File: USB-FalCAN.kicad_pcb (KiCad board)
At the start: 4 copper layers, 76.5 x 30.9 mm, 58 parts, among them J1 Conn_01x17_Pin, J10 CAN, J2 NC, J3 Conn_01x17_Pin, J4 USB2.0_16P, J5 Boot, J6 NC, J7 DE9_Receptacle, J8 RS-485/422-TX, J9 RS-422-RX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

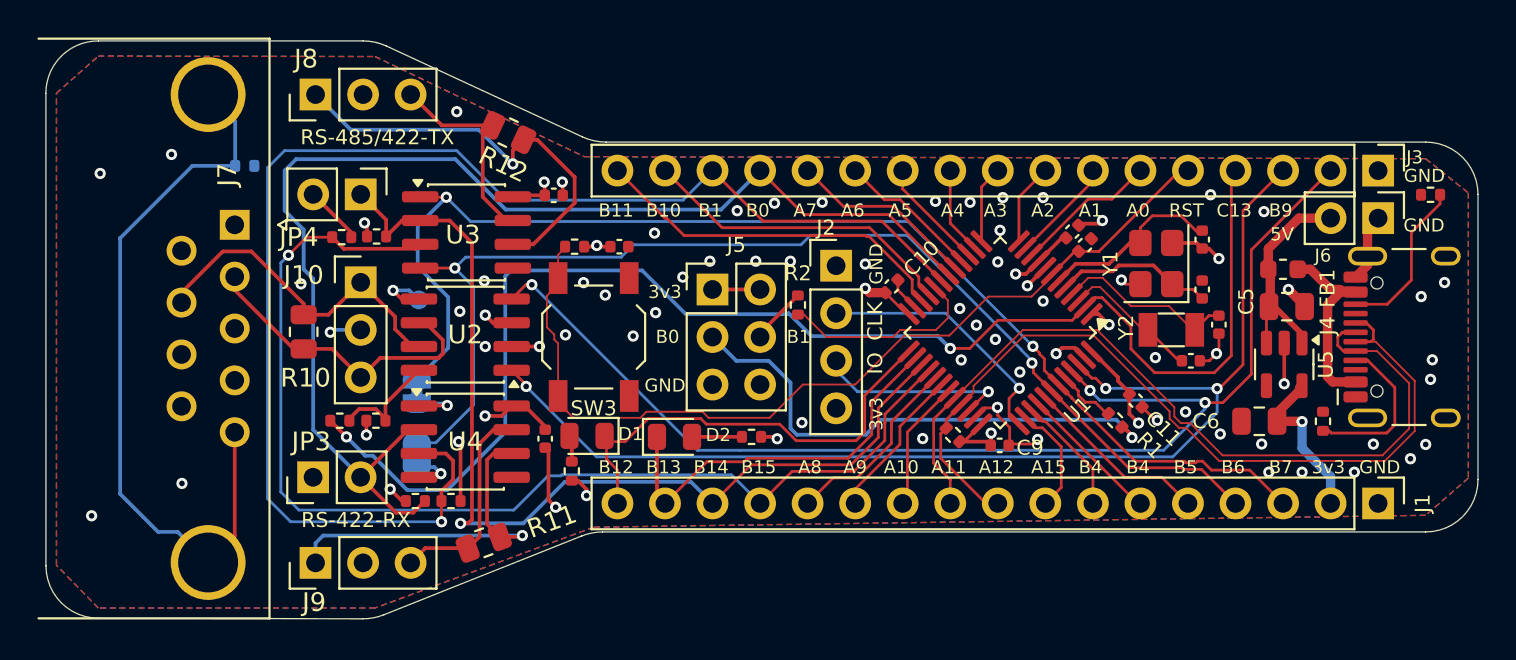
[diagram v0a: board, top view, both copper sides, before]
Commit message: Replace USB-TouCAN files with USB-FalCAN
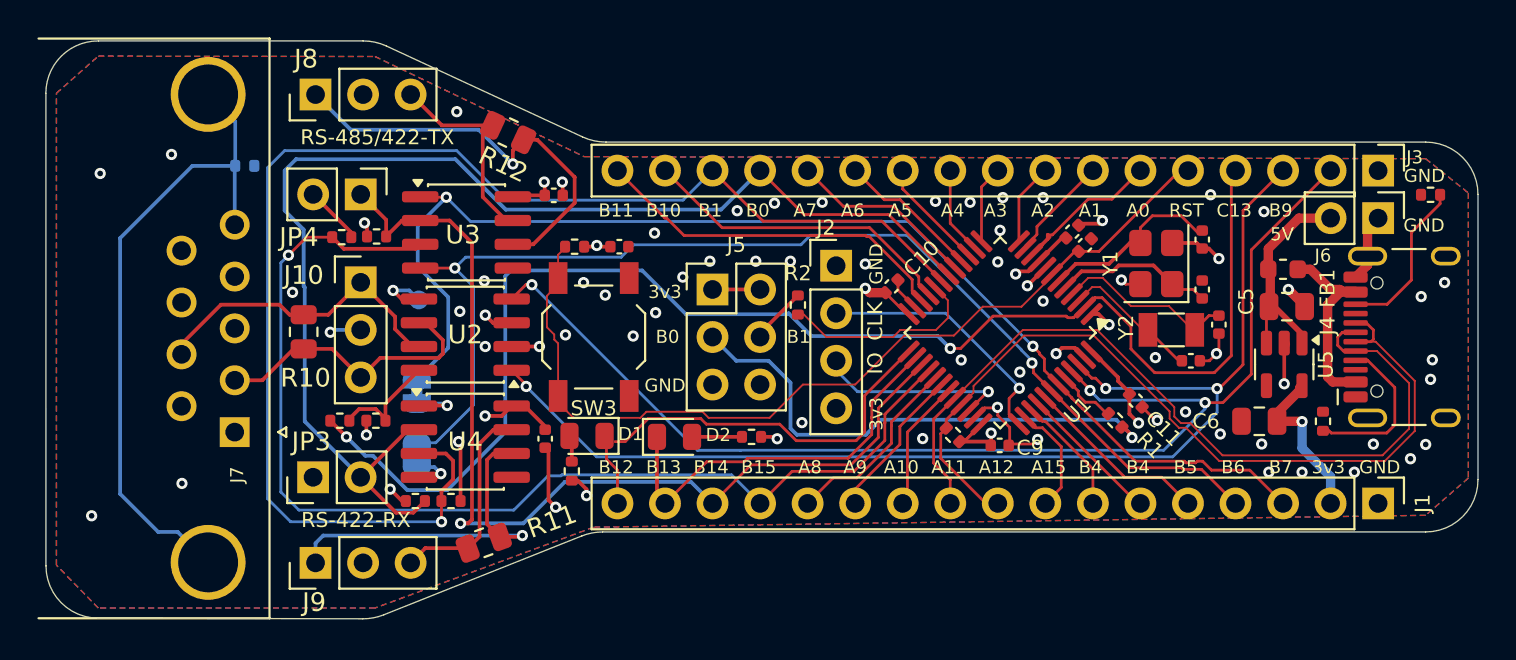
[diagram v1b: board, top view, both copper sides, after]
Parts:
- J7: footprint Connector_Dsub:DSUB-9_Pins_Horizontal_P2.77x2.84mm_EdgePinOffset7.70mm_Housed_MountingHolesOffset9.12mm -> Connector_Dsub:DSUB-9_Female_Horizontal_P2.77x2.84mm_EdgePinOffset7.70mm_Housed_MountingHolesOffset9.12mm
- moved J7 11.1 mm to (142.1, 78.7)
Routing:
- net Net-(J7-PAD): track 39.6 -> 35.2 mm
- net /CAN_H: track 18.0 -> 16.0 mm
- net /CAN_L: track 15.8 -> 14.5 mm
- net /PC13: track 75.2 -> 74.3 mm
- net GND: vias 70 -> 67

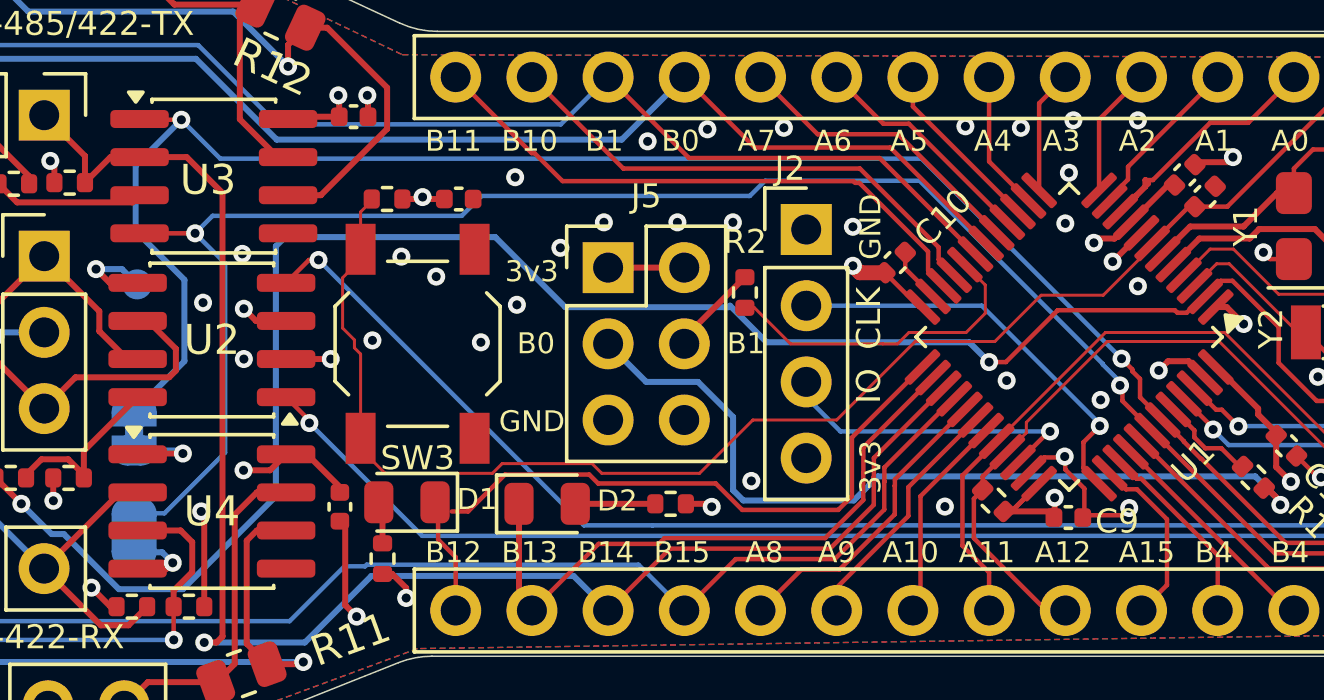
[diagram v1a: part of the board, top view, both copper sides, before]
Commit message: Improve silk
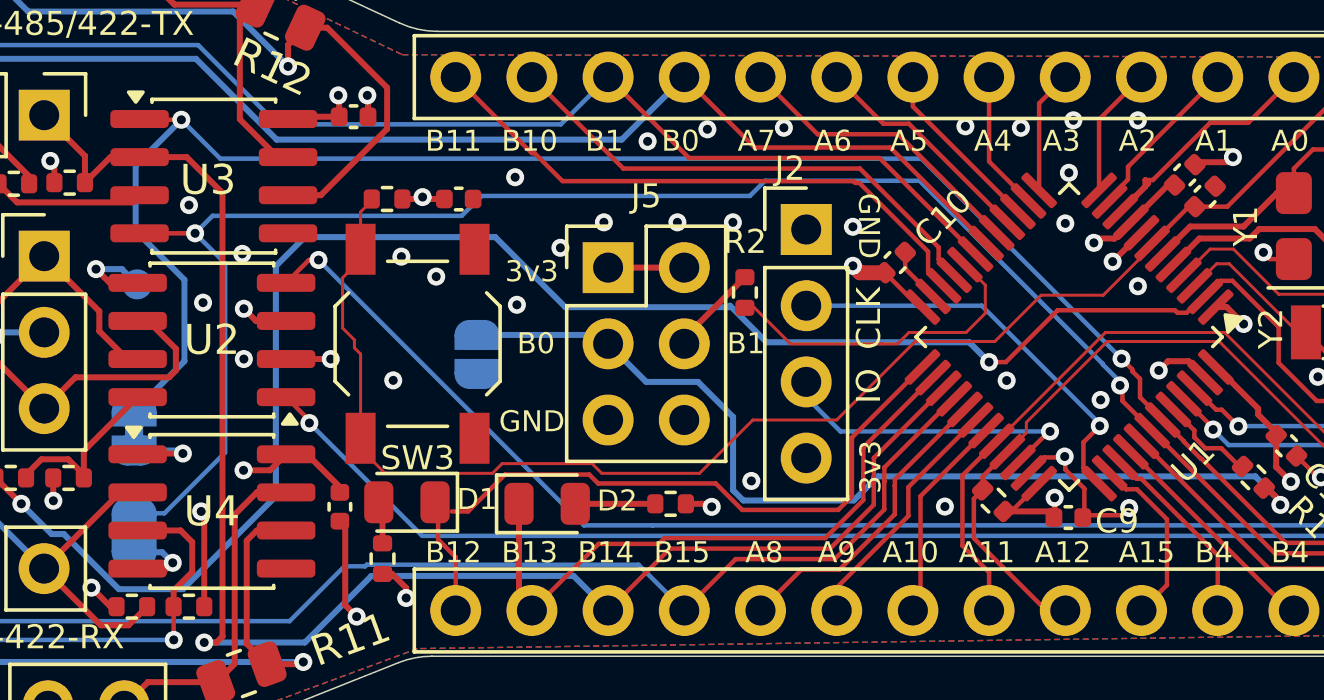
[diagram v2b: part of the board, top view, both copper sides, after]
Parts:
- added JP5: SolderJumper_2_Open, Jumper:SolderJumper-2_P1.3mm_Open_RoundedPad1.0x1.5mm, B.Cu at (163.3, 74.0)
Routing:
- net /BOOT0: track 27.5 -> 31.6 mm
- net +3V3: track 43.8 -> 42.3 mm
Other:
- board text added: "CAN TX"
- board text added: "RX"
- board text added: "SCL"
- board text added: "SDA"
- board text added: "TX"
